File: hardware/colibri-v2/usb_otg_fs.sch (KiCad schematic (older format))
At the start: 15 parts

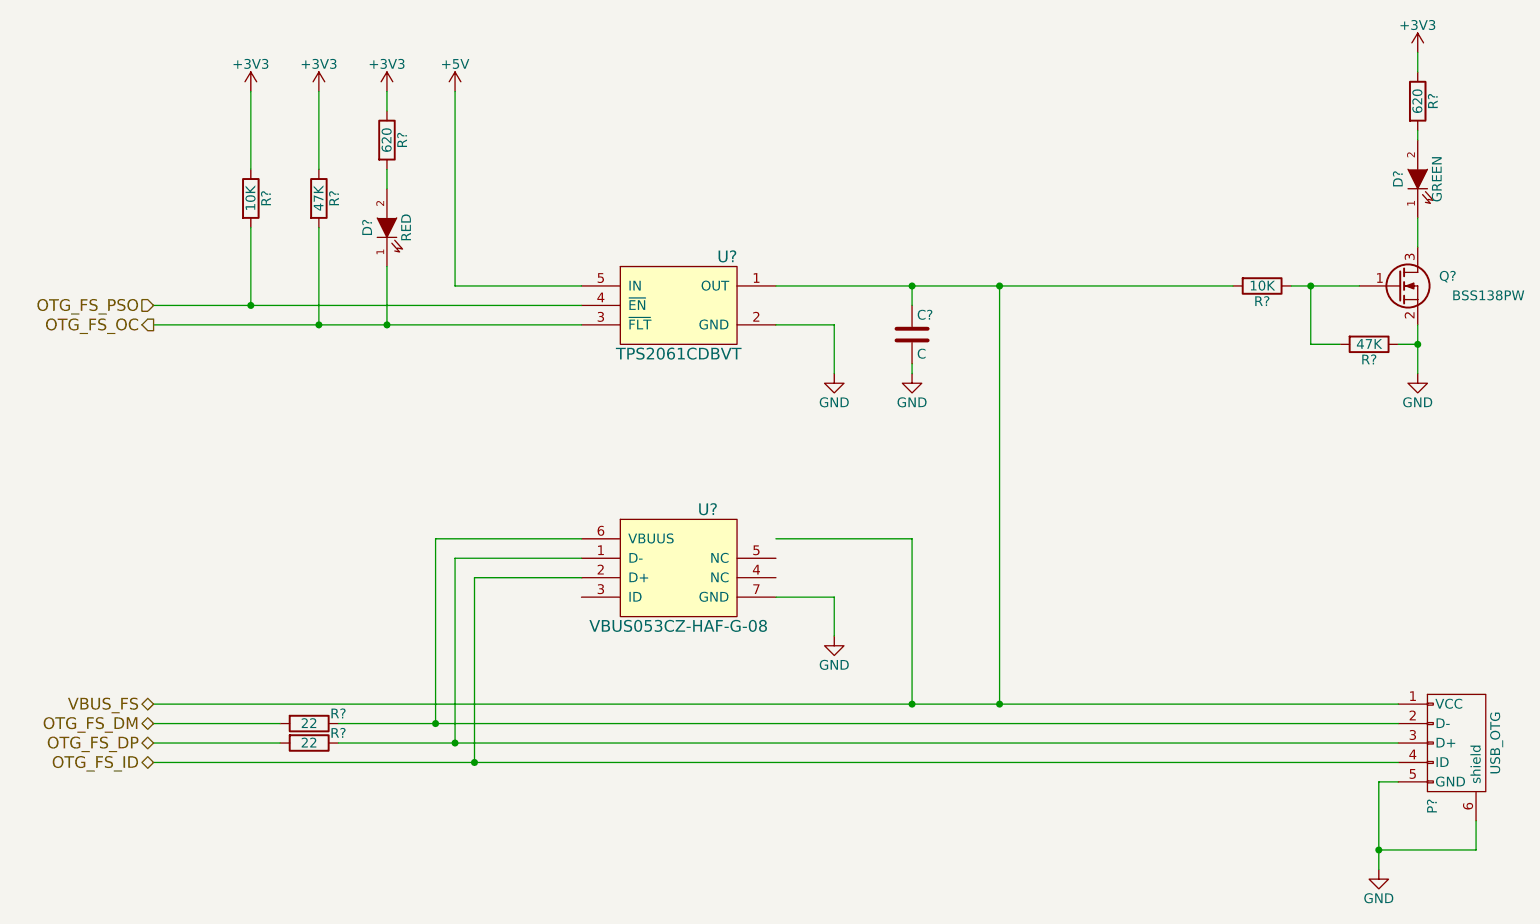
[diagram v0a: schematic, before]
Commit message: Added Wandboard USB Host
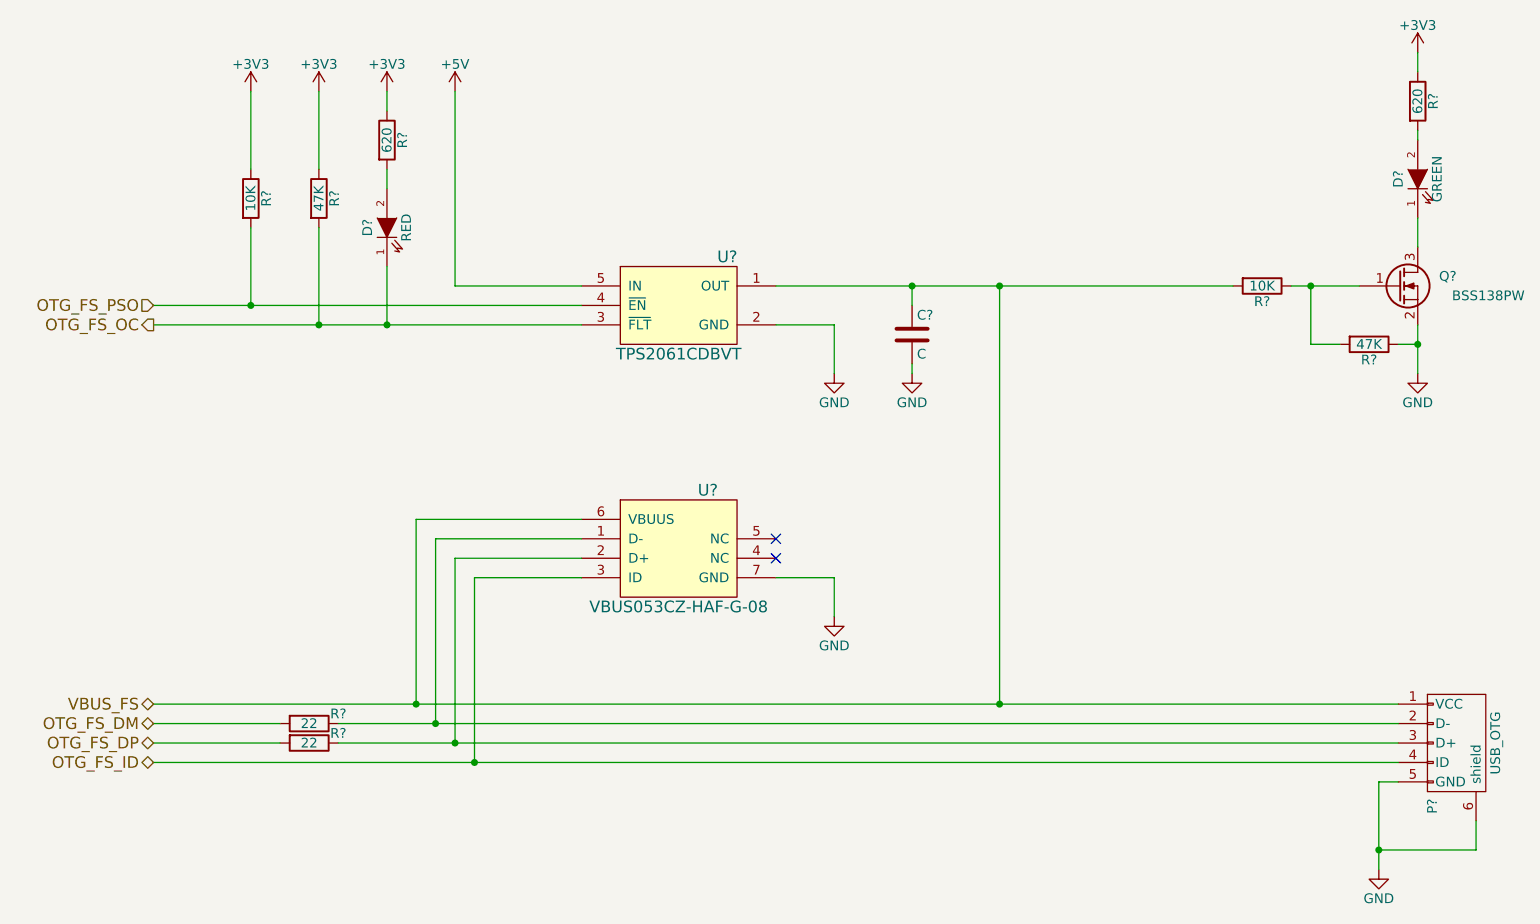
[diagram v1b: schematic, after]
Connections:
- net OTG_FS_ID: now also U?.3 (ID); no longer U?.2 (D+)
- net VBUS_FS: now also U?.6 (VBUUS)
- net at P?.2 (D-), R?.1: now also U?.1 (D-); no longer U?.6 (VBUUS)
- net at P?.3 (D+), R?.1: now also U?.2 (D+); no longer U?.1 (D-)
- no-connect marks 0 -> 2
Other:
- moved on the sheet: U?
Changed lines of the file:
@@
 $Descr A4 11693 8268
 encoding utf-8
-Sheet 7 21
+Sheet 19 22
 Title ""
 Date ""
@@
 L VBUS053CZ-HAF-G-08 U?
 U 1 1 5614ED91
-P 5300 4250
-F 0 "U?" H 5450 4550 60  0000 C CNN
-F 1 "VBUS053CZ-HAF-G-08" H 5300 3950 60  0000 C CNN
-F 2 "" H 5250 4950 60  0000 C CNN
-F 3 "" H 5250 4950 60  0000 C CNN
-	1    5300 4250
+P 5300 4150
+F 0 "U?" H 5450 4450 60  0000 C CNN
+F 1 "VBUS053CZ-HAF-G-08" H 5300 3850 60  0000 C CNN
+F 2 "" H 5250 4850 60  0000 C CNN
+F 3 "" H 5250 4850 60  0000 C CNN
+	1    5300 4150
 	1    0    0    -1
 $EndComp
@@
 L GND #PWR?
 U 1 1 5614EE16
-P 6100 4600
-F 0 "#PWR?" H 6100 4350 50  0001 C CNN
-F 1 "GND" H 6100 4450 50  0000 C CNN
-F 2 "" H 6100 4600 60  0000 C CNN
-F 3 "" H 6100 4600 60  0000 C CNN
-	1    6100 4600
+P 6100 4500
+F 0 "#PWR?" H 6100 4250 50  0001 C CNN
+F 1 "GND" H 6100 4350 50  0000 C CNN
+F 2 "" H 6100 4500 60  0000 C CNN
+F 3 "" H 6100 4500 60  0000 C CNN
+	1    6100 4500
 	1    0    0    -1
 $EndComp
@@
 	2600 5150 3250 5150
 Wire Wire Line
-	3550 5050 4050 5050
-Wire Wire Line
-	4050 5050 9000 5050
-Wire Wire Line
-	3550 5150 4150 5150
-Wire Wire Line
-	4150 5150 9000 5150
-Wire Wire Line
-	2600 4950 6500 4950
-Wire Wire Line
-	6500 4950 6950 4950
-Wire Wire Line
-	6950 4950 9000 4950
-Wire Wire Line
-	2600 5250 4250 5250
-Wire Wire Line
-	4250 5250 9000 5250
-Wire Wire Line
-	2600 2900 3100 2900
-Wire Wire Line
-	3100 2900 4800 2900
-Wire Wire Line
-	2600 3000 3450 3000
-Wire Wire Line
-	3450 3000 3800 3000
-Wire Wire Line
-	3800 3000 4800 3000
+	3550 5050 9000 5050
+Wire Wire Line
+	3550 5150 9000 5150
+Wire Wire Line
+	2600 4950 9000 4950
+Wire Wire Line
+	2600 5250 9000 5250
+Wire Wire Line
+	2600 2900 4800 2900
+Wire Wire Line
+	2600 3000 4800 3000
 Wire Wire Line
 	3100 1800 3100 2200
@@
 	9100 2450 9100 2600
 Wire Wire Line
-	9100 3000 9100 3100
-Wire Wire Line
-	9100 3100 9100 3250
-Wire Wire Line
-	8450 2800 8550 2800
-Wire Wire Line
-	8550 2800 8800 2800
-Wire Wire Line
-	5800 2800 6500 2800
-Wire Wire Line
-	6500 2800 6950 2800
-Wire Wire Line
-	6950 2800 8150 2800
+	9100 3000 9100 3250
+Wire Wire Line
+	8450 2800 8800 2800
+Wire Wire Line
+	5800 2800 8150 2800
 Wire Wire Line
 	6950 2800 6950 4950
@@
 Connection ~ 9100 3100
 Wire Wire Line
-	5800 4400 6100 4400
-Wire Wire Line
-	6100 4400 6100 4600
-Wire Wire Line
-	5800 4100 6500 4100
-Wire Wire Line
-	6500 4100 6500 4950
-Connection ~ 6500 4950
+	5800 4300 6100 4300
+Wire Wire Line
+	6100 4300 6100 4500
 Wire Wire Line
 	4800 4300 4250 4300
@@
 	9000 5350 8900 5350
 Wire Wire Line
-	8900 5350 8900 5700
-Wire Wire Line
-	8900 5700 8900 5800
+	8900 5350 8900 5800
 Wire Wire Line
 	9400 5550 9400 5700
@@
 Wire Wire Line
 	6100 3000 6100 3250
+NoConn ~ 5800 4100
+NoConn ~ 5800 4200
+Wire Wire Line
+	4800 4000 3950 4000
+Wire Wire Line
+	3950 4000 3950 4950
+Connection ~ 3950 4950
 $EndSCHEMATC

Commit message: Annotated Components
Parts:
- gave numbers to parts that had none: 15
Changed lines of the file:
@@
 $EndDescr
 $Comp
-L USB_OTG P?
+L USB_OTG P9
 U 1 1 5614ED84
 P 9300 5150
-F 0 "P?" H 9625 5025 50  0000 C CNN
+F 0 "P9" H 9625 5025 50  0000 C CNN
 F 1 "USB_OTG" H 9300 5350 50  0000 C CNN
 F 2 "" V 9250 5050 60  0000 C CNN
@@
 OTG_FS_PSO
 $Comp
-L VBUS053CZ-HAF-G-08 U?
+L VBUS053CZ-HAF-G-08 U18
 U 1 1 5614ED91
 P 5300 4150
-F 0 "U?" H 5450 4450 60  0000 C CNN
+F 0 "U18" H 5450 4450 60  0000 C CNN
 F 1 "VBUS053CZ-HAF-G-08" H 5300 3850 60  0000 C CNN
 F 2 "" H 5250 4850 60  0000 C CNN
@@
 $EndComp
 $Comp
-L R R?
+L R R118
 U 1 1 5614ED98
 P 3400 5050
-F 0 "R?" V 3350 5200 50  0000 C CNN
+F 0 "R118" V 3350 5200 50  0000 C CNN
 F 1 "22" V 3400 5050 50  0000 C CNN
 F 2 "" V 3330 5050 30  0000 C CNN
@@
 $EndComp
 $Comp
-L R R?
+L R R119
 U 1 1 5614ED9F
 P 3400 5150
-F 0 "R?" V 3350 5300 50  0000 C CNN
+F 0 "R119" V 3350 5300 50  0000 C CNN
 F 1 "22" V 3400 5150 50  0000 C CNN
 F 2 "" V 3330 5150 30  0000 C CNN
@@
 $EndComp
 $Comp
-L +3V3 #PWR?
+L +3V3 #PWR151
 U 1 1 5614EDA6
 P 3100 1800
-F 0 "#PWR?" H 3100 1650 50  0001 C CNN
+F 0 "#PWR151" H 3100 1650 50  0001 C CNN
 F 1 "+3V3" H 3100 1940 50  0000 C CNN
 F 2 "" H 3100 1800 60  0000 C CNN
@@
 $EndComp
 $Comp
-L R R?
+L R R117
 U 1 1 5614EDAC
 P 3100 2350
-F 0 "R?" V 3180 2350 50  0000 C CNN
+F 0 "R117" V 3180 2350 50  0000 C CNN
 F 1 "10K" V 3100 2350 50  0000 C CNN
 F 2 "" V 3030 2350 30  0000 C CNN
@@
 $EndComp
 $Comp
-L +3V3 #PWR?
+L +3V3 #PWR152
 U 1 1 5614EDB3
 P 3450 1800
-F 0 "#PWR?" H 3450 1650 50  0001 C CNN
+F 0 "#PWR152" H 3450 1650 50  0001 C CNN
 F 1 "+3V3" H 3450 1940 50  0000 C CNN
 F 2 "" H 3450 1800 60  0000 C CNN
@@
 $EndComp
 $Comp
-L R R?
+L R R120
 U 1 1 5614EDB9
 P 3450 2350
-F 0 "R?" V 3530 2350 50  0000 C CNN
+F 0 "R120" V 3530 2350 50  0000 C CNN
 F 1 "47K" V 3450 2350 50  0000 C CNN
 F 2 "" V 3380 2350 30  0000 C CNN
@@
 $EndComp
 $Comp
-L LED D?
+L LED D16
 U 1 1 5614EDC0
 P 3800 2500
-F 0 "D?" H 3800 2600 50  0000 C CNN
+F 0 "D16" H 3800 2600 50  0000 C CNN
 F 1 "RED" H 3800 2400 50  0000 C CNN
 F 2 "" H 3800 2500 60  0000 C CNN
@@
 $EndComp
 $Comp
-L R R?
+L R R121
 U 1 1 5614EDC7
 P 3800 2050
-F 0 "R?" V 3880 2050 50  0000 C CNN
+F 0 "R121" V 3880 2050 50  0000 C CNN
 F 1 "620" V 3800 2050 50  0000 C CNN
 F 2 "" V 3730 2050 30  0000 C CNN
@@
 $EndComp
 $Comp
-L +3V3 #PWR?
+L +3V3 #PWR153
 U 1 1 5614EDCE
 P 3800 1800
-F 0 "#PWR?" H 3800 1650 50  0001 C CNN
+F 0 "#PWR153" H 3800 1650 50  0001 C CNN
 F 1 "+3V3" H 3800 1940 50  0000 C CNN
 F 2 "" H 3800 1800 60  0000 C CNN
@@
 $EndComp
 $Comp
-L LED D?
+L LED D17
 U 1 1 5614EDD4
 P 9100 2250
-F 0 "D?" H 9100 2350 50  0000 C CNN
+F 0 "D17" H 9100 2350 50  0000 C CNN
 F 1 "GREEN" H 9100 2150 50  0000 C CNN
 F 2 "" H 9100 2250 60  0000 C CNN
@@
 $EndComp
 $Comp
-L R R?
+L R R124
 U 1 1 5614EDDB
 P 9100 1850
-F 0 "R?" V 9180 1850 50  0000 C CNN
+F 0 "R124" V 9180 1850 50  0000 C CNN
 F 1 "620" V 9100 1850 50  0000 C CNN
 F 2 "" V 9030 1850 30  0000 C CNN
@@
 $EndComp
 $Comp
-L +3V3 #PWR?
+L +3V3 #PWR159
 U 1 1 5614EDE2
 P 9100 1600
-F 0 "#PWR?" H 9100 1450 50  0001 C CNN
+F 0 "#PWR159" H 9100 1450 50  0001 C CNN
 F 1 "+3V3" H 9100 1740 50  0000 C CNN
 F 2 "" H 9100 1600 60  0000 C CNN
@@
 $EndComp
 $Comp
-L Q_NMOS_GSD Q?
+L Q_NMOS_GSD Q9
 U 1 1 5614EDE8
 P 9000 2800
-F 0 "Q?" H 9300 2850 50  0000 R CNN
+F 0 "Q9" H 9300 2850 50  0000 R CNN
 F 1 "BSS138PW" H 9650 2750 50  0000 R CNN
 F 2 "" H 9200 2900 29  0000 C CNN
@@
 $EndComp
 $Comp
-L GND #PWR?
+L GND #PWR160
 U 1 1 5614EDEF
 P 9100 3250
-F 0 "#PWR?" H 9100 3000 50  0001 C CNN
+F 0 "#PWR160" H 9100 3000 50  0001 C CNN
 F 1 "GND" H 9100 3100 50  0000 C CNN
 F 2 "" H 9100 3250 60  0000 C CNN
@@
 $EndComp
 $Comp
-L R R?
+L R R122
 U 1 1 5614EDF5
 P 8300 2800
-F 0 "R?" V 8380 2800 50  0000 C CNN
+F 0 "R122" V 8380 2800 50  0000 C CNN
 F 1 "10K" V 8300 2800 50  0000 C CNN
 F 2 "" V 8230 2800 30  0000 C CNN
@@
 $EndComp
 $Comp
-L R R?
+L R R123
 U 1 1 5614EDFC
 P 8850 3100
-F 0 "R?" V 8930 3100 50  0000 C CNN
+F 0 "R123" V 8930 3100 50  0000 C CNN
 F 1 "47K" V 8850 3100 50  0000 C CNN
 F 2 "" V 8780 3100 30  0000 C CNN
@@
 $EndComp
 $Comp
-L C C?
+L C C89
 U 1 1 5614EE03
 P 6500 3050
-F 0 "C?" H 6525 3150 50  0000 L CNN
+F 0 "C89" H 6525 3150 50  0000 L CNN
 F 1 "C" H 6525 2950 50  0000 L CNN
 F 2 "" H 6538 2900 30  0000 C CNN
@@
 $EndComp
 $Comp
-L GND #PWR?
+L GND #PWR157
 U 1 1 5614EE0A
 P 6500 3250
-F 0 "#PWR?" H 6500 3000 50  0001 C CNN
+F 0 "#PWR157" H 6500 3000 50  0001 C CNN
 F 1 "GND" H 6500 3100 50  0000 C CNN
 F 2 "" H 6500 3250 60  0000 C CNN
@@
 $EndComp
 $Comp
-L GND #PWR?
+L GND #PWR155
 U 1 1 5614EE10
 P 6100 3250
-F 0 "#PWR?" H 6100 3000 50  0001 C CNN
+F 0 "#PWR155" H 6100 3000 50  0001 C CNN
 F 1 "GND" H 6100 3100 50  0000 C CNN
 F 2 "" H 6100 3250 60  0000 C CNN
@@
 $EndComp
 $Comp
-L GND #PWR?
+L GND #PWR156
 U 1 1 5614EE16
 P 6100 4500
-F 0 "#PWR?" H 6100 4250 50  0001 C CNN
+F 0 "#PWR156" H 6100 4250 50  0001 C CNN
 F 1 "GND" H 6100 4350 50  0000 C CNN
 F 2 "" H 6100 4500 60  0000 C CNN
@@
 Connection ~ 4050 5050
 $Comp
-L GND #PWR?
+L GND #PWR158
 U 1 1 5614EE59
 P 8900 5800
-F 0 "#PWR?" H 8900 5550 50  0001 C CNN
+F 0 "#PWR158" H 8900 5550 50  0001 C CNN
 F 1 "GND" H 8900 5650 50  0000 C CNN
 F 2 "" H 8900 5800 60  0000 C CNN
@@
 Connection ~ 8900 5700
 $Comp
-L +5V #PWR?
+L +5V #PWR154
 U 1 1 5614EE65
 P 4150 1800
-F 0 "#PWR?" H 4150 1650 50  0001 C CNN
+F 0 "#PWR154" H 4150 1650 50  0001 C CNN
 F 1 "+5V" H 4150 1940 50  0000 C CNN
 F 2 "" H 4150 1800 60  0000 C CNN
@@
 $EndComp
 $Comp
-L TPS2061CDBVT U?
+L TPS2061CDBVT U17
 U 1 1 5614EE6B
 P 5300 2900
-F 0 "U?" H 5550 3150 60  0000 C CNN
+F 0 "U17" H 5550 3150 60  0000 C CNN
 F 1 "TPS2061CDBVT" H 5300 2650 60  0000 C CNN
 F 2 "" H 5300 2700 60  0000 C CNN

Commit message: Work on hardware
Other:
- note added: "or use TPS2061CDBVT"
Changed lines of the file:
@@
 	3950 4000 3950 4950
 Connection ~ 3950 4950
+Text Notes 4950 2500 0    60   ~ 0
+or use TPS2061CDBVT
 $EndSCHEMATC

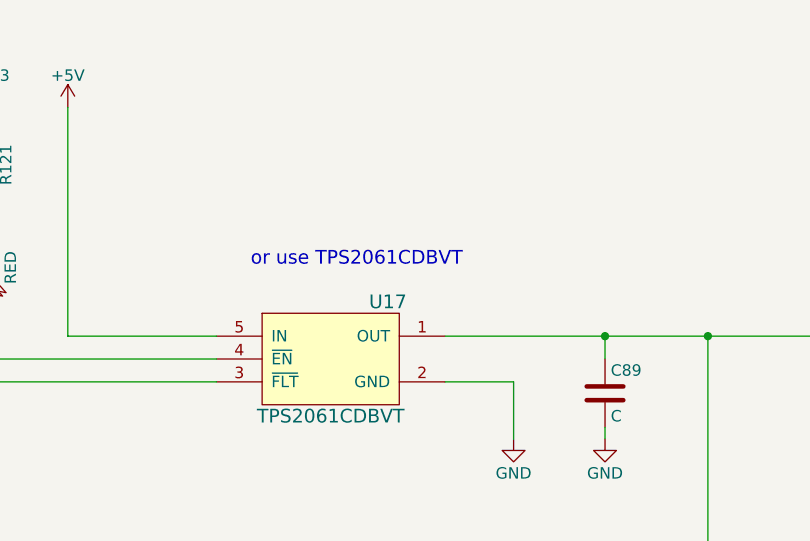
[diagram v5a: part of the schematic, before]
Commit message: Reworked the buttons/leds sheet
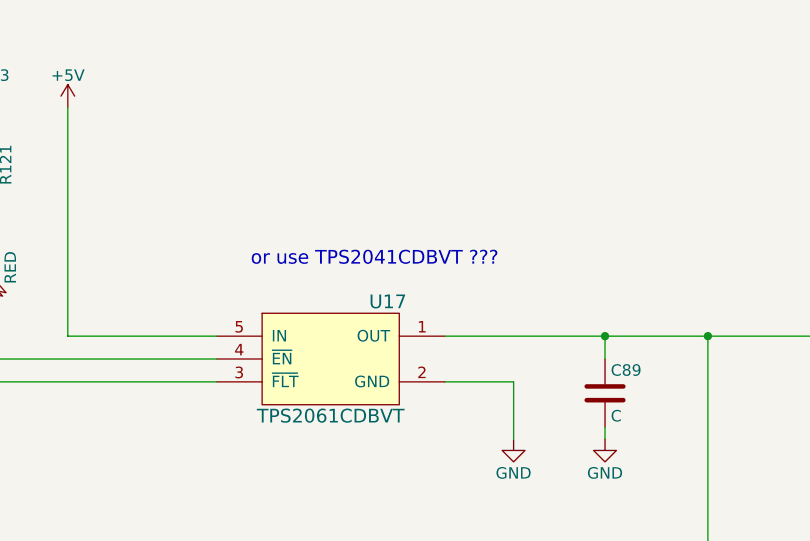
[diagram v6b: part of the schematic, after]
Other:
- note added: "or use TPS2041CDBVT ???"
- note removed: "or use TPS2061CDBVT"
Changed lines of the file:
@@
 Connection ~ 3950 4950
 Text Notes 4950 2500 0    60   ~ 0
-or use TPS2061CDBVT
+or use TPS2041CDBVT ???
 $EndSCHEMATC

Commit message: Re-annotated schematic
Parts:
- renumbered C89 to C87, R117 to R120, R118 to R121, R119 to R122, R120 to R123, R121 to R124, R122 to R125, R123 to R126, R124 to R127
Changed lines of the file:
@@
 $EndComp
 $Comp
-L R R118
+L R R121
 U 1 1 5614ED98
 P 3400 5050
-F 0 "R118" V 3350 5200 50  0000 C CNN
+F 0 "R121" V 3350 5200 50  0000 C CNN
 F 1 "22" V 3400 5050 50  0000 C CNN
 F 2 "" V 3330 5050 30  0000 C CNN
@@
 $EndComp
 $Comp
-L R R119
+L R R122
 U 1 1 5614ED9F
 P 3400 5150
-F 0 "R119" V 3350 5300 50  0000 C CNN
+F 0 "R122" V 3350 5300 50  0000 C CNN
 F 1 "22" V 3400 5150 50  0000 C CNN
 F 2 "" V 3330 5150 30  0000 C CNN
@@
 $EndComp
 $Comp
-L +3V3 #PWR0153
+L +3V3 #PWR149
 U 1 1 5614EDA6
 P 3100 1800
-F 0 "#PWR0153" H 3100 1650 50  0001 C CNN
+F 0 "#PWR149" H 3100 1650 50  0001 C CNN
 F 1 "+3V3" H 3100 1940 50  0000 C CNN
 F 2 "" H 3100 1800 60  0000 C CNN
@@
 $EndComp
 $Comp
-L R R117
+L R R120
 U 1 1 5614EDAC
 P 3100 2350
-F 0 "R117" V 3180 2350 50  0000 C CNN
+F 0 "R120" V 3180 2350 50  0000 C CNN
 F 1 "10K" V 3100 2350 50  0000 C CNN
 F 2 "" V 3030 2350 30  0000 C CNN
@@
 $EndComp
 $Comp
-L +3V3 #PWR0154
+L +3V3 #PWR150
 U 1 1 5614EDB3
 P 3450 1800
-F 0 "#PWR0154" H 3450 1650 50  0001 C CNN
+F 0 "#PWR150" H 3450 1650 50  0001 C CNN
 F 1 "+3V3" H 3450 1940 50  0000 C CNN
 F 2 "" H 3450 1800 60  0000 C CNN
@@
 $EndComp
 $Comp
-L R R120
+L R R123
 U 1 1 5614EDB9
 P 3450 2350
-F 0 "R120" V 3530 2350 50  0000 C CNN
+F 0 "R123" V 3530 2350 50  0000 C CNN
 F 1 "47K" V 3450 2350 50  0000 C CNN
 F 2 "" V 3380 2350 30  0000 C CNN
@@
 $EndComp
 $Comp
-L R R121
+L R R124
 U 1 1 5614EDC7
 P 3800 2050
-F 0 "R121" V 3880 2050 50  0000 C CNN
+F 0 "R124" V 3880 2050 50  0000 C CNN
 F 1 "620" V 3800 2050 50  0000 C CNN
 F 2 "" V 3730 2050 30  0000 C CNN
@@
 $EndComp
 $Comp
-L +3V3 #PWR0155
+L +3V3 #PWR151
 U 1 1 5614EDCE
 P 3800 1800
-F 0 "#PWR0155" H 3800 1650 50  0001 C CNN
+F 0 "#PWR151" H 3800 1650 50  0001 C CNN
 F 1 "+3V3" H 3800 1940 50  0000 C CNN
 F 2 "" H 3800 1800 60  0000 C CNN
@@
 $EndComp
 $Comp
-L R R124
+L R R127
 U 1 1 5614EDDB
 P 9100 1850
-F 0 "R124" V 9180 1850 50  0000 C CNN
+F 0 "R127" V 9180 1850 50  0000 C CNN
 F 1 "620" V 9100 1850 50  0000 C CNN
 F 2 "" V 9030 1850 30  0000 C CNN
@@
 $EndComp
 $Comp
-L +3V3 #PWR0156
+L +3V3 #PWR157
 U 1 1 5614EDE2
 P 9100 1600
-F 0 "#PWR0156" H 9100 1450 50  0001 C CNN
+F 0 "#PWR157" H 9100 1450 50  0001 C CNN
 F 1 "+3V3" H 9100 1740 50  0000 C CNN
 F 2 "" H 9100 1600 60  0000 C CNN
@@
 $EndComp
 $Comp
-L GND #PWR0157
+L GND #PWR158
 U 1 1 5614EDEF
 P 9100 3250
-F 0 "#PWR0157" H 9100 3000 50  0001 C CNN
+F 0 "#PWR158" H 9100 3000 50  0001 C CNN
 F 1 "GND" H 9100 3100 50  0000 C CNN
 F 2 "" H 9100 3250 60  0000 C CNN
@@
 $EndComp
 $Comp
-L R R122
+L R R125
 U 1 1 5614EDF5
 P 8300 2800
-F 0 "R122" V 8380 2800 50  0000 C CNN
+F 0 "R125" V 8380 2800 50  0000 C CNN
 F 1 "10K" V 8300 2800 50  0000 C CNN
 F 2 "" V 8230 2800 30  0000 C CNN
@@
 $EndComp
 $Comp
-L R R123
+L R R126
 U 1 1 5614EDFC
 P 8850 3100
-F 0 "R123" V 8930 3100 50  0000 C CNN
+F 0 "R126" V 8930 3100 50  0000 C CNN
 F 1 "47K" V 8850 3100 50  0000 C CNN
 F 2 "" V 8780 3100 30  0000 C CNN
@@
 $EndComp
 $Comp
-L C C89
+L C C87
 U 1 1 5614EE03
 P 6500 3050
-F 0 "C89" H 6525 3150 50  0000 L CNN
+F 0 "C87" H 6525 3150 50  0000 L CNN
 F 1 "C" H 6525 2950 50  0000 L CNN
 F 2 "" H 6538 2900 30  0000 C CNN
@@
 $EndComp
 $Comp
-L GND #PWR0158
+L GND #PWR155
 U 1 1 5614EE0A
 P 6500 3250
-F 0 "#PWR0158" H 6500 3000 50  0001 C CNN
+F 0 "#PWR155" H 6500 3000 50  0001 C CNN
 F 1 "GND" H 6500 3100 50  0000 C CNN
 F 2 "" H 6500 3250 60  0000 C CNN
@@
 $EndComp
 $Comp
-L GND #PWR0159
+L GND #PWR153
 U 1 1 5614EE10
 P 6100 3250
-F 0 "#PWR0159" H 6100 3000 50  0001 C CNN
+F 0 "#PWR153" H 6100 3000 50  0001 C CNN
 F 1 "GND" H 6100 3100 50  0000 C CNN
 F 2 "" H 6100 3250 60  0000 C CNN
@@
 $EndComp
 $Comp
-L GND #PWR0160
+L GND #PWR154
 U 1 1 5614EE16
 P 6100 4500
-F 0 "#PWR0160" H 6100 4250 50  0001 C CNN
+F 0 "#PWR154" H 6100 4250 50  0001 C CNN
 F 1 "GND" H 6100 4350 50  0000 C CNN
 F 2 "" H 6100 4500 60  0000 C CNN
@@
 Connection ~ 4050 5050
 $Comp
-L GND #PWR0161
+L GND #PWR156
 U 1 1 5614EE59
 P 8900 5800
-F 0 "#PWR0161" H 8900 5550 50  0001 C CNN
+F 0 "#PWR156" H 8900 5550 50  0001 C CNN
 F 1 "GND" H 8900 5650 50  0000 C CNN
 F 2 "" H 8900 5800 60  0000 C CNN
@@
 Connection ~ 8900 5700
 $Comp
-L +5V #PWR0162
+L +5V #PWR152
 U 1 1 5614EE65
 P 4150 1800
-F 0 "#PWR0162" H 4150 1650 50  0001 C CNN
+F 0 "#PWR152" H 4150 1650 50  0001 C CNN
 F 1 "+5V" H 4150 1940 50  0000 C CNN
 F 2 "" H 4150 1800 60  0000 C CNN
